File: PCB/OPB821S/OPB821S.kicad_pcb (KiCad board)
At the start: 2 copper layers, 21 parts, among them J1 Conn_02x02, J10 Screw_Terminal_01x02, J2 Conn_02x02, J3 Conn_01x02, J4 Conn_02x05_Odd_Even, J7 LEMO5, J8 Screw_Terminal_01x03, J9 LEMO5, U1 74HC14, U2 OP249

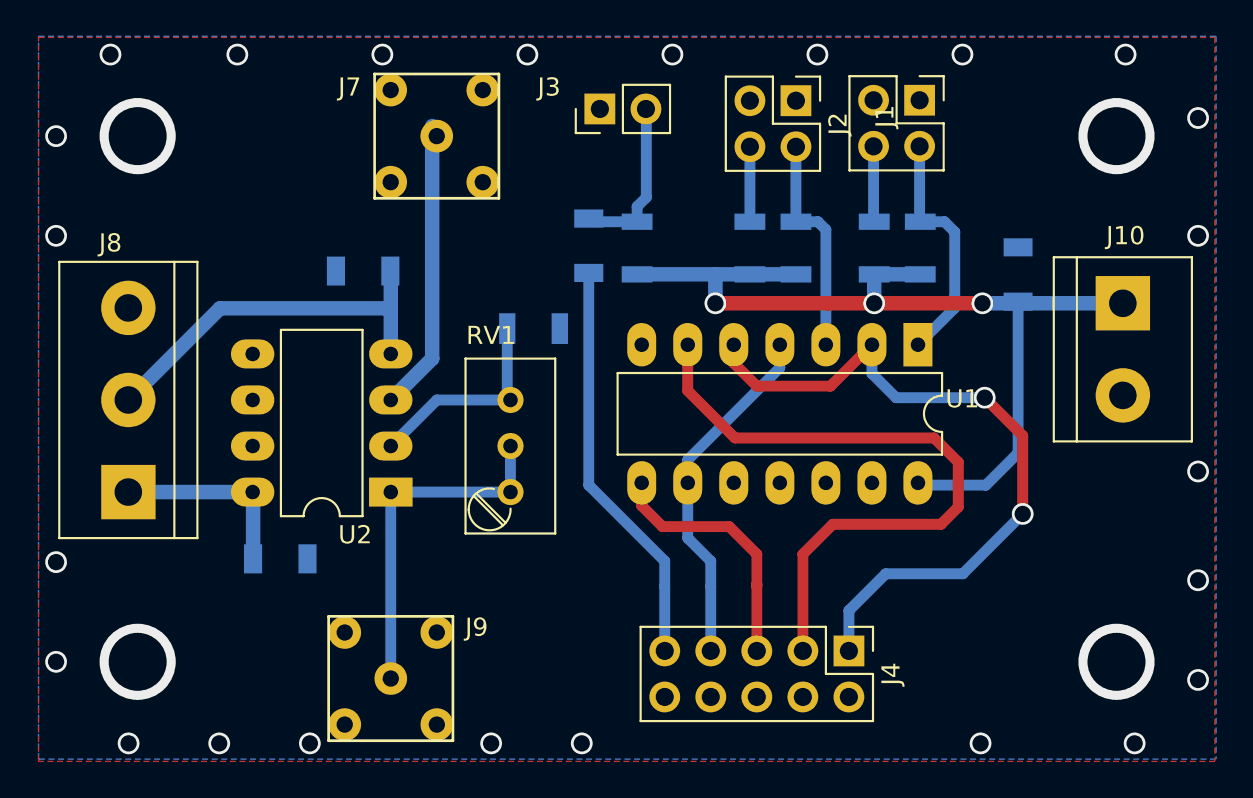
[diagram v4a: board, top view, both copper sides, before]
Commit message: integrate guard ring into the ground plane
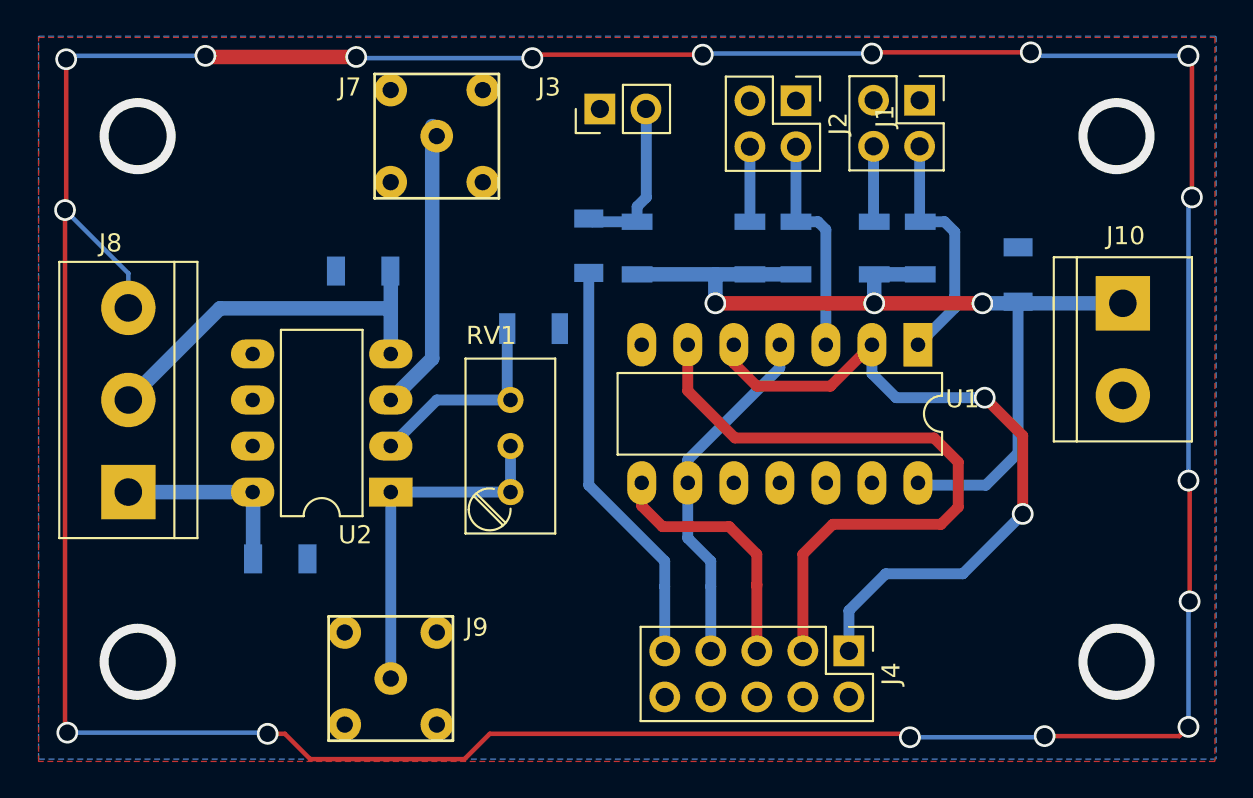
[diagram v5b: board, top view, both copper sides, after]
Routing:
- net GND: track 22.6 -> 229.4 mm, vias 0 -> 17
- net (no net): vias 28 -> 4
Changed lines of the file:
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@@
     (thickness 1.6)
     (drawings 13)
-    (tracks 128)
+    (tracks 162)
     (zones 0)
     (modules 21)
@@
   )
   (layers
-    (0 F.Cu signal)
+    (0 F.Cu signal hide)
     (31 B.Cu signal)
     (32 B.Adhes user)
@@
   )
   (setup
-    (last_trace_width 0.25)
+    (last_trace_width 0.8)
     (user_trace_width 0.25)
     (user_trace_width 0.5)
@@
   (gr_line (start 202 47) (end 202 87) (angle 90) (layer F.Fab) (width 0.2))
   (gr_line (start 137 47) (end 202 47) (angle 90) (layer F.Fab) (width 0.2))
-  (via (at 152 86) (size 1.2) (drill 0.9) (layers F.Cu B.Cu) (net 0))
   (via (at 142.5 52.5) (size 4.2) (drill 3.2) (layers F.Cu B.Cu) (net 0))
-  (via (at 167 86) (size 1.2) (drill 0.9) (layers F.Cu B.Cu) (net 0))
-  (via (at 162 86) (size 1.2) (drill 0.9) (layers F.Cu B.Cu) (net 0))
-  (via (at 180 48) (size 1.2) (drill 0.9) (layers F.Cu B.Cu) (net 0))
-  (via (at 188 48) (size 1.2) (drill 0.9) (layers F.Cu B.Cu) (net 0))
-  (via (at 138 76) (size 1.2) (drill 0.9) (layers F.Cu B.Cu) (net 0))
-  (via (at 138 81.5) (size 1.2) (drill 0.9) (layers F.Cu B.Cu) (net 0))
-  (via (at 142 86) (size 1.2) (drill 0.9) (layers F.Cu B.Cu) (net 0))
-  (via (at 147 86) (size 1.2) (drill 0.9) (layers F.Cu B.Cu) (net 0))
-  (via (at 189 86) (size 1.2) (drill 0.9) (layers F.Cu B.Cu) (net 0))
-  (via (at 197.5 86) (size 1.2) (drill 0.9) (layers F.Cu B.Cu) (net 0))
-  (via (at 201 71) (size 1.2) (drill 0.9) (layers F.Cu B.Cu) (net 0))
-  (via (at 201 77) (size 1.2) (drill 0.9) (layers F.Cu B.Cu) (net 0))
-  (via (at 201 82.5) (size 1.2) (drill 0.9) (layers F.Cu B.Cu) (net 0))
-  (via (at 201 58) (size 1.2) (drill 0.9) (layers F.Cu B.Cu) (net 0))
-  (via (at 201 51.5) (size 1.2) (drill 0.9) (layers F.Cu B.Cu) (net 0))
-  (via (at 197 48) (size 1.2) (drill 0.9) (layers F.Cu B.Cu) (net 0))
-  (via (at 141 48) (size 1.2) (drill 0.9) (layers F.Cu B.Cu) (net 0))
-  (via (at 172 48) (size 1.2) (drill 0.9) (layers F.Cu B.Cu) (net 0))
-  (via (at 164 48) (size 1.2) (drill 0.9) (layers F.Cu B.Cu) (net 0))
-  (via (at 138 58) (size 1.2) (drill 0.9) (layers F.Cu B.Cu) (net 0))
-  (via (at 138 52.5) (size 1.2) (drill 0.9) (layers F.Cu B.Cu) (net 0))
-  (via (at 156 48) (size 1.2) (drill 0.9) (layers F.Cu B.Cu) (net 0))
-  (via (at 148 48) (size 1.2) (drill 0.9) (layers F.Cu B.Cu) (net 0))
   (via (at 142.5 81.5) (size 4.2) (drill 3.2) (layers F.Cu B.Cu) (net 0))
   (via (at 196.5 81.5) (size 4.2) (drill 3.2) (layers F.Cu B.Cu) (net 0))
   (via (at 196.5 52.5) (size 4.2) (drill 3.2) (layers F.Cu B.Cu) (net 0))
+  (segment (start 138.4935 56.769) (end 138.557 56.7055) (width 0.25) (layer F.Cu) (net 1))
+  (segment (start 138.4935 85.2805) (end 138.4935 56.769) (width 0.25) (layer F.Cu) (net 1))
+  (segment (start 138.6205 85.4075) (end 138.4935 85.2805) (width 0.25) (layer F.Cu) (net 1))
+  (via (at 138.6205 85.4075) (size 1.2) (drill 0.9) (layers F.Cu B.Cu) (net 1))
+  (segment (start 149.606 85.4075) (end 138.6205 85.4075) (width 0.25) (layer B.Cu) (net 1))
+  (segment (start 149.6695 85.471) (end 149.606 85.4075) (width 0.25) (layer B.Cu) (net 1))
+  (via (at 149.6695 85.471) (size 1.2) (drill 0.9) (layers F.Cu B.Cu) (net 1))
+  (segment (start 150.622 85.471) (end 149.6695 85.471) (width 0.25) (layer F.Cu) (net 1))
+  (segment (start 152.019 86.868) (end 150.622 85.471) (width 0.25) (layer F.Cu) (net 1))
+  (segment (start 160.528 86.868) (end 152.019 86.868) (width 0.25) (layer F.Cu) (net 1))
+  (segment (start 161.925 85.471) (end 160.528 86.868) (width 0.25) (layer F.Cu) (net 1))
+  (segment (start 184.912 85.471) (end 161.925 85.471) (width 0.25) (layer F.Cu) (net 1))
+  (segment (start 185.1025 85.6615) (end 184.912 85.471) (width 0.25) (layer F.Cu) (net 1))
+  (via (at 185.1025 85.6615) (size 1.2) (drill 0.9) (layers F.Cu B.Cu) (net 1))
+  (segment (start 192.4685 85.6615) (end 185.1025 85.6615) (width 0.25) (layer B.Cu) (net 1))
+  (segment (start 192.532 85.598) (end 192.4685 85.6615) (width 0.25) (layer B.Cu) (net 1))
+  (via (at 192.532 85.598) (size 1.2) (drill 0.9) (layers F.Cu B.Cu) (net 1))
+  (segment (start 199.9615 85.598) (end 192.532 85.598) (width 0.25) (layer F.Cu) (net 1))
+  (segment (start 200.4695 85.09) (end 199.9615 85.598) (width 0.25) (layer F.Cu) (net 1))
+  (via (at 200.4695 85.09) (size 1.2) (drill 0.9) (layers F.Cu B.Cu) (net 1))
+  (segment (start 200.4695 78.232) (end 200.4695 85.09) (width 0.25) (layer B.Cu) (net 1))
+  (segment (start 200.533 78.1685) (end 200.4695 78.232) (width 0.25) (layer B.Cu) (net 1))
+  (via (at 200.533 78.1685) (size 1.2) (drill 0.9) (layers F.Cu B.Cu) (net 1))
+  (segment (start 200.533 71.5645) (end 200.533 78.1685) (width 0.25) (layer F.Cu) (net 1))
+  (segment (start 200.4695 71.501) (end 200.533 71.5645) (width 0.25) (layer F.Cu) (net 1))
+  (via (at 200.4695 71.501) (size 1.2) (drill 0.9) (layers F.Cu B.Cu) (net 1))
+  (segment (start 200.4695 56.0705) (end 200.4695 71.501) (width 0.25) (layer B.Cu) (net 1))
+  (segment (start 200.66 55.88) (end 200.4695 56.0705) (width 0.25) (layer B.Cu) (net 1))
+  (via (at 200.66 55.88) (size 1.2) (drill 0.9) (layers F.Cu B.Cu) (net 1))
+  (segment (start 200.66 48.26) (end 200.66 55.88) (width 0.25) (layer F.Cu) (net 1))
+  (segment (start 200.4695 48.0695) (end 200.66 48.26) (width 0.25) (layer F.Cu) (net 1))
+  (via (at 200.4695 48.0695) (size 1.2) (drill 0.9) (layers F.Cu B.Cu) (net 1))
+  (segment (start 191.9605 48.0695) (end 200.4695 48.0695) (width 0.25) (layer B.Cu) (net 1))
+  (segment (start 191.77 47.879) (end 191.9605 48.0695) (width 0.25) (layer B.Cu) (net 1))
+  (via (at 191.77 47.879) (size 1.2) (drill 0.9) (layers F.Cu B.Cu) (net 1))
+  (segment (start 183.0705 47.879) (end 191.77 47.879) (width 0.25) (layer F.Cu) (net 1))
+  (segment (start 183.007 47.9425) (end 183.0705 47.879) (width 0.25) (layer F.Cu) (net 1))
+  (via (at 183.007 47.9425) (size 1.2) (drill 0.9) (layers F.Cu B.Cu) (net 1))
+  (segment (start 173.736 47.9425) (end 183.007 47.9425) (width 0.25) (layer B.Cu) (net 1))
+  (segment (start 173.6725 48.006) (end 173.736 47.9425) (width 0.25) (layer B.Cu) (net 1))
+  (via (at 173.6725 48.006) (size 1.2) (drill 0.9) (layers F.Cu B.Cu) (net 1))
+  (segment (start 164.465 48.006) (end 173.6725 48.006) (width 0.25) (layer F.Cu) (net 1))
+  (segment (start 164.2745 48.1965) (end 164.465 48.006) (width 0.25) (layer F.Cu) (net 1))
+  (via (at 164.2745 48.1965) (size 1.2) (drill 0.9) (layers F.Cu B.Cu) (net 1))
+  (segment (start 154.6225 48.1965) (end 164.2745 48.1965) (width 0.25) (layer B.Cu) (net 1))
+  (segment (start 154.559 48.133) (end 154.6225 48.1965) (width 0.25) (layer B.Cu) (net 1))
+  (via (at 154.559 48.133) (size 1.2) (drill 0.9) (layers F.Cu B.Cu) (net 1))
+  (segment (start 146.304 48.133) (end 154.559 48.133) (width 0.8) (layer F.Cu) (net 1))
+  (segment (start 146.2405 48.0695) (end 146.304 48.133) (width 0.25) (layer F.Cu) (net 1))
+  (via (at 146.2405 48.0695) (size 1.2) (drill 0.9) (layers F.Cu B.Cu) (net 1))
+  (segment (start 138.7475 48.0695) (end 146.2405 48.0695) (width 0.25) (layer B.Cu) (net 1))
+  (segment (start 138.557 48.26) (end 138.7475 48.0695) (width 0.25) (layer B.Cu) (net 1))
+  (via (at 138.557 48.26) (size 1.2) (drill 0.9) (layers F.Cu B.Cu) (net 1))
+  (segment (start 138.557 56.515) (end 138.557 48.26) (width 0.25) (layer F.Cu) (net 1))
+  (segment (start 138.4935 56.5785) (end 138.557 56.515) (width 0.25) (layer F.Cu) (net 1))
+  (via (at 138.4935 56.5785) (size 1.2) (drill 0.9) (layers F.Cu B.Cu) (net 1))
+  (segment (start 141.986 60.071) (end 138.4935 56.5785) (width 0.25) (layer B.Cu) (net 1))
+  (segment (start 141.986 61.976) (end 141.986 60.071) (width 0.25) (layer B.Cu) (net 1))
   (segment (start 171.577 80.899) (end 171.577 77.343) (width 0.6) (layer B.Cu) (net 1))
   (segment (start 167.386 71.755) (end 171.577 75.946) (width 0.6) (layer B.Cu) (net 1))
@@
   (segment (start 178.816 60.124) (end 176.276 60.124) (width 0.8) (layer B.Cu) (net 16))
   (segment (start 185.674 60.124) (end 183.134 60.124) (width 0.8) (layer B.Cu) (net 16))
-  (segment (start 196.85 61.722) (end 189.103 61.722) (width 0.8) (layer B.Cu) (net 16))
+  (segment (start 196.85 61.722) (end 189.103 61.722) (width 0.8) (layer B.Cu) (net 16) (status 10))
   (segment (start 189.103 61.722) (end 183.134 61.722) (width 0.8) (layer F.Cu) (net 16))
   (via (at 189.103 61.722) (size 1.2) (drill 0.9) (layers F.Cu B.Cu) (net 16))
   (zone (net 1) (net_name GND) (layer F.Cu) (hatch edge 0.508)
-    (connect_pads (clearance 0.508))
+    (connect_pads thru_hole_only (clearance 0.508))
     (min_thickness 0.254)
     (fill yes (arc_segments 16) (thermal_gap 0.508) (thermal_bridge_width 0.508))
